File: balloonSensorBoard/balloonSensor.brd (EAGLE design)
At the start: 100 x 80 mm, 36 parts, among them IC1 MCP601OT, IC10 MCP601OT, IC6 MCP601OT, IC7 MCP601OT, U1 ARDUINO-MEGAPRO

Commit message: updated .sch, .brd
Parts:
- removed +9V1: 500 ohm, rcl:R1206
- removed C6, C7: 10uF, resistor:CT3216
- removed LD1085: (no value), v-reg:TO220L1
- removed LED3: (no value), SparkFun:LED3MM
- removed U$3: XBEE-1B3, SparkFun:XBEE-SMD
- added C2: 100nF, resistor:CT3216
- added C3: 10uF, resistor:CT3216
- added JP1: (no value), SparkFun:1X04_LONGPADS
- added LD1117: V_REG_317SMD, SparkFun:SOT223
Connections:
- removed net N$19: +9V1.2, LED3.K
- net +3V3: now also JP1.1, U1.3.3V; no longer U$3.1
- net +9V: now also C2.+, LD1117.3, U1.VIN; no longer C6.+, LD1085.3
- net GND: now also C2.-, C3.-, JP1.4, LD1117.1, U1.GND@4; no longer +9V1.1, C6.-, C7.-, LD1085.1, U$3.10
- net N$13: now also JP1.3; no longer U$3.3
- net N$5: now also JP1.2; no longer U$3.2
- net V+: now also C3.+, LD1117.2; no longer C7.+, LD1085.2, LED3.A
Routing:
- net GND: track 199.9 -> 172.8 mm
- net +9V: track 69.0 -> 50.0 mm
- net N$19: track 4.33 -> 0.00 mm
- net V+: track 207.9 -> 205.4 mm

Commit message: updated .sch, .brd
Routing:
- net GND: track 172.8 -> 118.0 mm
- net +9V: track 50.0 -> 6.21 mm
- net V+: track 205.4 -> 180.5 mm
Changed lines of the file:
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@@
 <wire x1="57.912" y1="44.704" x2="60.198" y2="44.704" width="0.254" layer="16"/>
 <wire x1="57.912" y1="44.704" x2="57.68" y2="44.98" width="0.254" layer="16"/>
-<wire x1="34.544" y1="18.288" x2="22.352" y2="30.48" width="0.254" layer="16"/>
-<wire x1="37.592" y1="18.288" x2="34.544" y2="18.288" width="0.254" layer="16"/>
-<wire x1="22.352" y1="30.48" x2="21.59" y2="30.56" width="0.254" layer="16"/>
 <wire x1="60.96" y1="29.718" x2="60.96" y2="26.706" width="0.254" layer="1"/>
 <wire x1="61.722" y1="30.48" x2="60.96" y2="29.718" width="0.254" layer="1"/>
@@
 <wire x1="34.29" y1="57.15" x2="33.528" y2="56.388" width="0.254" layer="1"/>
 <wire x1="34.29" y1="60.96" x2="34.29" y2="57.15" width="0.254" layer="1"/>
-<wire x1="22.098" y1="28.956" x2="32.004" y2="28.956" width="0.254" layer="1"/>
-<wire x1="32.004" y1="28.956" x2="32.766" y2="28.956" width="0.254" layer="1"/>
-<wire x1="22.098" y1="30.48" x2="22.098" y2="28.956" width="0.254" layer="1"/>
-<wire x1="22.098" y1="30.48" x2="21.59" y2="30.56" width="0.254" layer="1"/>
 <wire x1="34.29" y1="33.528" x2="33.528" y2="34.29" width="0.254" layer="1"/>
 <wire x1="34.29" y1="30.48" x2="34.29" y2="33.528" width="0.254" layer="1"/>
 <wire x1="33.528" y1="29.718" x2="34.29" y2="30.48" width="0.254" layer="1"/>
 <wire x1="33.528" y1="34.29" x2="33.02" y2="34.773" width="0.254" layer="1"/>
-<wire x1="58.674" y1="29.718" x2="57.912" y2="30.48" width="0.254" layer="1"/>
-<wire x1="59.69" y1="20.574" x2="59.436" y2="20.574" width="0.254" layer="1"/>
-<wire x1="58.674" y1="21.5265" x2="58.674" y2="25.146" width="0.254" layer="1"/>
-<wire x1="58.674" y1="25.146" x2="58.674" y2="29.718" width="0.254" layer="1"/>
-<wire x1="57.912" y1="30.48" x2="57.785" y2="30.963" width="0.254" layer="1"/>
-<wire x1="32.004" y1="23.622" x2="32.766" y2="22.86" width="0.254" layer="1"/>
-<wire x1="32.004" y1="28.956" x2="32.004" y2="23.622" width="0.254" layer="1"/>
 <wire x1="34.29" y1="54.864" x2="33.528" y2="55.626" width="0.254" layer="1"/>
 <wire x1="34.29" y1="33.528" x2="34.29" y2="54.864" width="0.254" layer="1"/>
-<wire x1="60.96" y1="25.908" x2="60.96" y2="26.706" width="0.254" layer="1"/>
-<wire x1="60.198" y1="25.146" x2="60.96" y2="25.908" width="0.254" layer="1"/>
-<wire x1="58.674" y1="25.146" x2="60.198" y2="25.146" width="0.254" layer="1"/>
-<wire x1="58.674" y1="21.5265" x2="59.436" y2="20.574" width="0.254" layer="1"/>
 <contactref element="U$1" pad="FIGV+/E2V-"/>
 <contactref element="R2" pad="2"/>
@@
 <wire x1="10.16" y1="-95.25" x2="5.08" y2="-95.25" width="0" layer="19" extent="1-1"/>
 <wire x1="9.42" y1="-70.38" x2="3.81" y2="-82.586" width="0" layer="19" extent="1-1"/>
-<wire x1="34.544" y1="18.288" x2="9.42" y2="-70.38" width="0" layer="19" extent="16-16"/>
-<wire x1="33.528" y1="29.718" x2="32.766" y2="28.956" width="0" layer="19" extent="1-1"/>
+<wire x1="21.59" y1="30.56" x2="9.42" y2="-70.38" width="0" layer="19" extent="1-1"/>
+<wire x1="33.528" y1="29.718" x2="21.59" y2="30.56" width="0" layer="19" extent="1-1"/>
 <wire x1="33.528" y1="56.388" x2="33.528" y2="55.626" width="0" layer="19" extent="1-1"/>
 <wire x1="20.066" y1="62.23" x2="34.29" y2="60.96" width="0" layer="19" extent="1-1"/>
-<wire x1="58.674" y1="21.5265" x2="37.592" y2="18.288" width="0" layer="19" extent="1-16"/>
-<wire x1="60.198" y1="21.59" x2="59.69" y2="20.574" width="0" layer="19" extent="1-16"/>
+<wire x1="57.785" y1="30.963" x2="34.29" y2="30.48" width="0" layer="19" extent="1-1"/>
+<wire x1="60.96" y1="29.718" x2="57.785" y2="30.963" width="0" layer="19" extent="1-1"/>
+<wire x1="60.198" y1="21.59" x2="60.96" y2="26.706" width="0" layer="19" extent="1-16"/>
 </signal>
 <signal name="V+">
@@
 <contactref element="IC7" pad="5"/>
 <contactref element="IC10" pad="5"/>
-<wire x1="42.672" y1="15.24" x2="40.64" y2="17.272" width="0.254" layer="16"/>
-<wire x1="54.737" y1="15.24" x2="42.672" y2="15.24" width="0.254" layer="16"/>
+<wire x1="42.672" y1="15.24" x2="40.64" y2="17.272" width="0" layer="19" extent="1-16"/>
+<wire x1="54.737" y1="15.24" x2="42.672" y2="15.24" width="0" layer="19" extent="1-16"/>
 <wire x1="54.483" y1="16.256" x2="54.737" y2="15.24" width="0.254" layer="16"/>
 <wire x1="28.448" y1="44.704" x2="28.448" y2="41.656" width="0.254" layer="1"/>
@@
 <wire x1="53.848" y1="44.704" x2="54.08" y2="44.98" width="0.254" layer="16"/>
 <wire x1="54.61" y1="15.24" x2="54.737" y2="15.24" width="0.3048" layer="16"/>
-<wire x1="54.737" y1="15.24" x2="64.77" y2="15.24" width="0.3048" layer="16"/>
+<wire x1="54.737" y1="15.24" x2="64.77" y2="15.24" width="0" layer="19" extent="1-16"/>
 <wire x1="64.77" y1="15.24" x2="64.77" y2="23.622" width="0.3048" layer="16"/>
 <wire x1="75.438" y1="31.242" x2="73.152" y2="31.242" width="0.254" layer="1"/>
@@
 <wire x1="21.59" y1="35.56" x2="25.4" y2="35.56" width="0.254" layer="16"/>
 <wire x1="26.416" y1="36.576" x2="27.305" y2="36.195" width="0.254" layer="16"/>
-<wire x1="60.96" y1="18.288" x2="61.976" y2="17.272" width="0.254" layer="16"/>
-<wire x1="43.688" y1="18.288" x2="44.704" y2="18.288" width="0.254" layer="16"/>
-<wire x1="44.704" y1="18.288" x2="60.96" y2="18.288" width="0.254" layer="16"/>
-<wire x1="44.704" y1="18.288" x2="27.432" y2="35.56" width="0.254" layer="16"/>
-<wire x1="27.432" y1="35.56" x2="27.305" y2="36.195" width="0.254" layer="16"/>
 <contactref element="U1" pad="VIN"/>
 <contactref element="C2" pad="+"/>
@@
 <wire x1="-11.6586" y1="-121.2088" x2="-12.57" y2="-125.73" width="0" layer="19" extent="1-1"/>
 <wire x1="39.37" y1="13.97" x2="-11.6586" y2="-121.2088" width="0" layer="19" extent="1-1"/>
-<wire x1="43.688" y1="18.288" x2="39.37" y2="13.97" width="0" layer="19" extent="16-16"/>
+<wire x1="27.305" y1="36.195" x2="39.37" y2="13.97" width="0" layer="19" extent="1-1"/>
 </signal>
 <signal name="N$38">

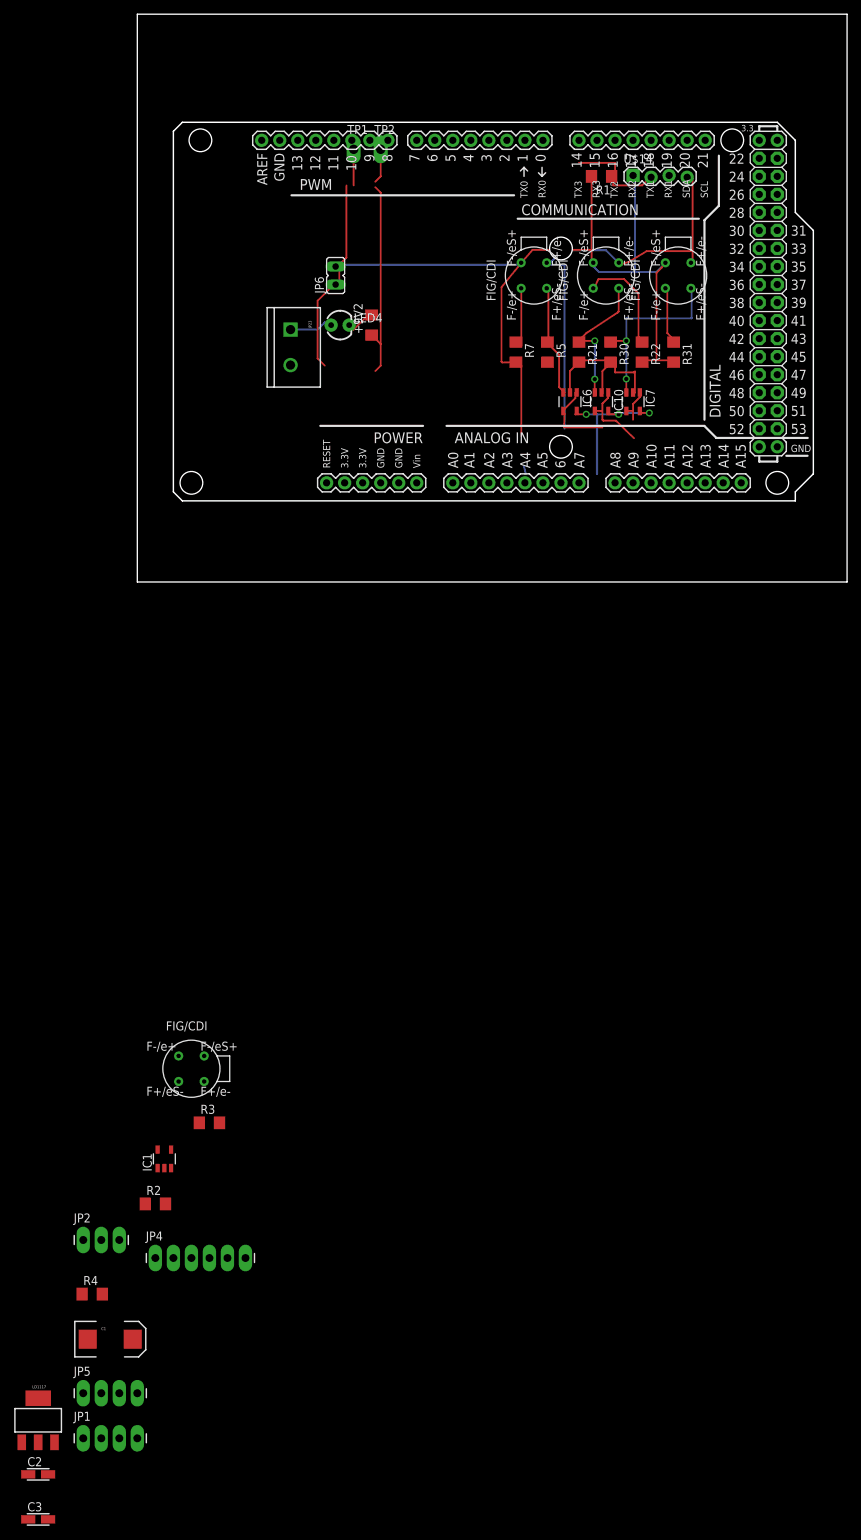
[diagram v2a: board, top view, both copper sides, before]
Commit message: added sensors and miscellaneous parts and routed board
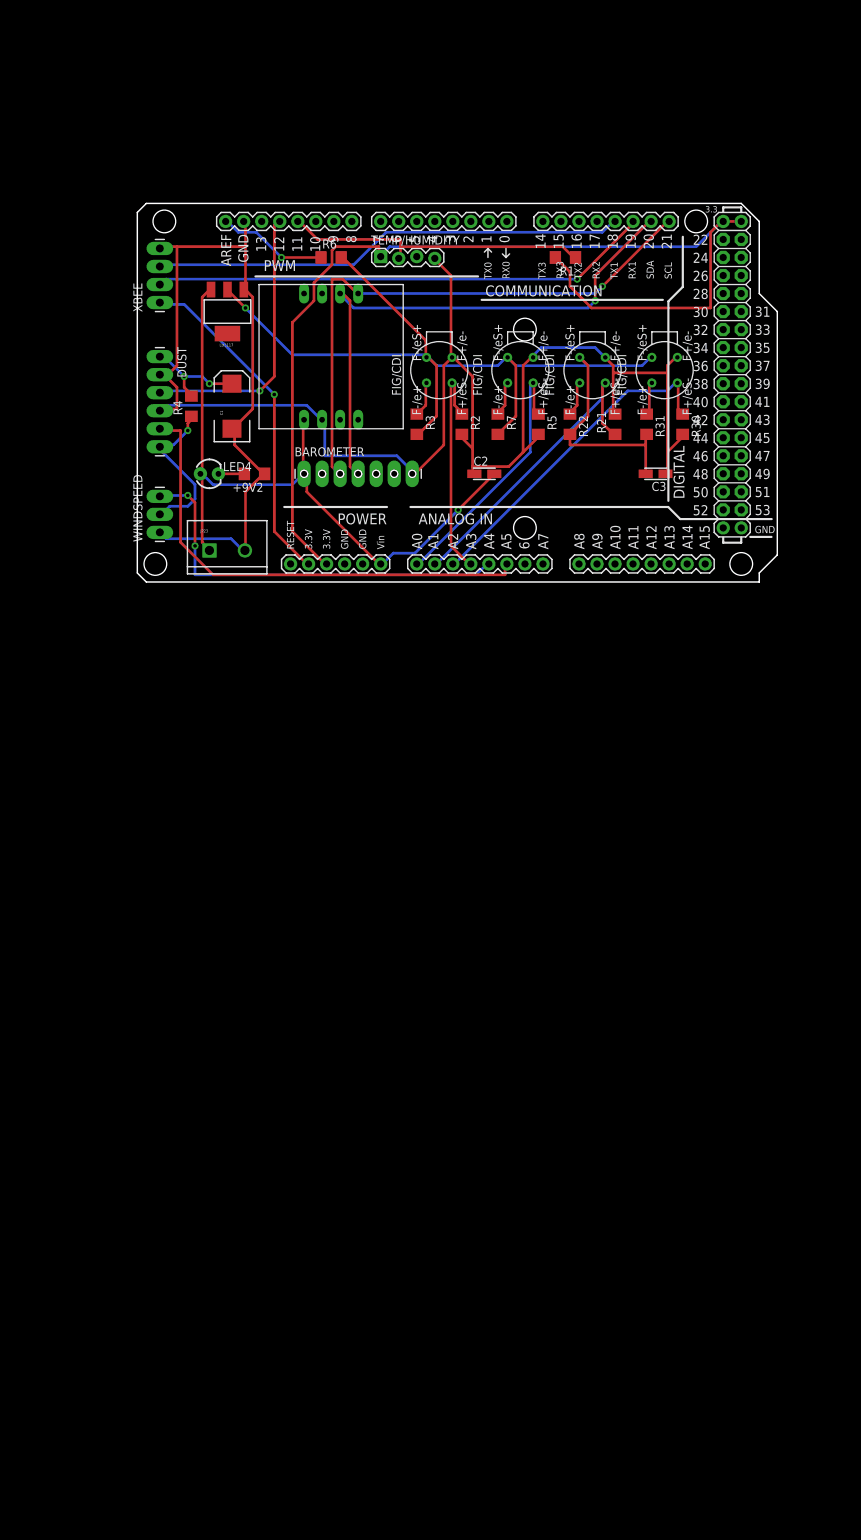
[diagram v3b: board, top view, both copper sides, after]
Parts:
- removed IC1, IC10, IC6, IC7: MCP601OT, linear:SOT23-5
- removed JP1, JP5: (no value), SparkFun:1X04_LONGPADS
- removed JP2: (no value), SparkFun:1X03_LONGPADS
- removed JP4: (no value), SparkFun:1X06_LONGPADS
- removed JP6: (no value), jumper:JP1
- removed TP1, TP2: TPPAD1-13Y, testpad:P1-13Y
- removed U$1, U$9: E2V Ozone, ricardo:SR-4
- removed U$13: E2V, ricardo:SR-4
- removed U$14: RHT03, ricardo:1X04_LOCK
- added BAROMETER: (no value), SparkFun:1X07_LONGPADS
- added CO: E2V, ricardo:SR-4
- added COMPASS: COMPASS, balloonshield:COMPASS
- added DUST: (no value), SparkFun:1X06_LONGPADS
- added O3, VOC: E2V Ozone, ricardo:SR-4
- added R6: 1k, rcl:R1206
- added TEMP/HUMIDITY: RHT03, ricardo:1X04_LOCK
- added WINDSPEED: (no value), SparkFun:1X03_LONGPADS
- added XBEE: (no value), SparkFun:1X04_LONGPADS
- moved C3 171.1 mm to (73.0, 15.2), turned to 180 degrees
- moved LD1117 158.5 mm to (12.7, 38.1), turned to 180 degrees
- moved C2 154.4 mm to (48.9, 15.2)
- moved C1 132.6 mm to (13.3, 24.8), turned to 90 degrees
- moved R4 125.9 mm to (7.62, 24.8), turned to 90 degrees
- moved R2 118.0 mm to (45.7, 22.2), turned to 270 degrees
- moved R3 102.7 mm to (39.4, 22.2), turned to 270 degrees
- moved JP23 33.1 mm to (10.2, 4.45), turned to 0 degrees
- moved LED4 27.9 mm to (10.2, 15.2)
- moved +9V2 26.7 mm to (16.5, 15.2), turned to 180 degrees
- moved R22 14.4 mm to (61.0, 22.2)
- moved R30 14.4 mm to (76.8, 22.2)
- moved NO2 13.5 mm to (54.0, 29.8)
- moved R1 12.5 mm to (60.3, 45.7)
- moved U1 12.5 mm to (0.00, 0.00)
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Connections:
- removed net N$12: JP5.3, U1.20
- removed net N$20: JP5.4, U1.21
- removed net N$48: IC10.1, IC10.4, U1.A1
- removed net N$52: IC6.1, IC6.4, U1.A0
- removed net N$9: IC7.1, IC7.4, U1.A2
- new net 5V: R1.2, TEMP/HUMIDITY.VDD, U1.5V@0, U1.5V@1, U1.5V@2
- new net SCL: BAROMETER.3, COMPASS.SCL, U1.21
- new net SDA: BAROMETER.4, COMPASS.SDA, U1.20
- net +3V3: now also XBEE.1; no longer JP1.1, JP5.2
- net +5V: now also DUST.6, WINDSPEED.2; no longer JP2.2, JP4.6
- net +9V: now also BAROMETER.1, COMPASS.VIN
- net 3: now also TEMP/HUMIDITY.DATA; no longer U$14.DATA
- net GND: now also BAROMETER.7, CO.FIGV+/E2V-, COMPASS.GND, DUST.2, DUST.4, O3.FIGV+/E2V-, TEMP/HUMIDITY.GND, VOC.FIGV+/E2V-, WINDSPEED.1, XBEE.4; no longer IC1.2, IC10.2, IC6.2, IC7.2, JP1.4, JP2.1, JP4.2, JP4.4, JP5.1, TP2.TP, U$1.FIGV+/E2V-, U$13.FIGV+/E2V-, U$14.GND, U$9.FIGV+/E2V-
- net N$1: now also VOC.FIGSIG/E2VH+; no longer U$1.FIGSIG/E2VH+
- net N$10: now also DUST.3; no longer JP4.3
- net N$11: now also DUST.5; no longer JP4.5
- net N$13: now also XBEE.3; no longer JP1.3
- net N$2: now also U1.A3, VOC.FIGV+/E2VSIG; no longer IC1.3, U$1.FIGV+/E2VSIG
- net N$38: now also CO.FIGSIG/E2VH+; no longer U$13.FIGSIG/E2VH+
- net N$4: now also R6.1, U1.AREF; no longer IC1.1, IC1.4, U1.A3
- net N$45: now also O3.FIGSIG/E2VH+; no longer U$9.FIGSIG/E2VH+
- net N$47: now also CO.FIGV+/E2VSIG, U1.A1; no longer IC10.3, U$13.FIGV+/E2VSIG
- net N$5: now also XBEE.2; no longer JP1.2
- net N$50: now also U1.A0; no longer IC6.3
- net N$55: now also O3.FIGV+/E2VSIG, U1.A2; no longer IC7.3, U$9.FIGV+/E2VSIG
- net N$7: now also WINDSPEED.3; no longer JP2.3
- net N$8: now also DUST.1; no longer JP4.1
- net V+: now also CO.FIGG/E2VS+, O3.FIGG/E2VS+, R6.2, VOC.FIGG/E2VS+; no longer IC1.5, IC10.5, IC6.5, IC7.5, JP6.1, JP6.2, R1.2, TP1.TP, U$1.FIGG/E2VS+, U$13.FIGG/E2VS+, U$14.VDD, U$9.FIGG/E2VS+
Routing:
- net GND: track 118.0 -> 277.2 mm
- net 5V: track 0.00 -> 148.9 mm
- net +9V: track 6.21 -> 100.6 mm, vias 0 -> 1
- net SCL: track 0.00 -> 80.5 mm, vias 0 -> 1
- net SDA: track 0.00 -> 78.8 mm, vias 0 -> 1
- net N$5: track 0.00 -> 70.6 mm, vias 0 -> 1
- net N$11: track 0.00 -> 68.1 mm
- net N$13: track 0.00 -> 66.7 mm
- net N$7: track 0.00 -> 57.6 mm, vias 0 -> 2
- net +3V3: track 0.00 -> 47.5 mm, vias 0 -> 1
- net N$10: track 0.00 -> 39.4 mm, vias 0 -> 1
- net V+: track 180.5 -> 141.9 mm, vias 3 -> 1
- net N$2: track 0.00 -> 32.0 mm
- net 3: track 14.6 -> 43.6 mm
- net N$47: track 20.5 -> 44.2 mm, vias 2 -> 0
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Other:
- board size 100 x 80 mm -> 90.2 x 53.3 mm

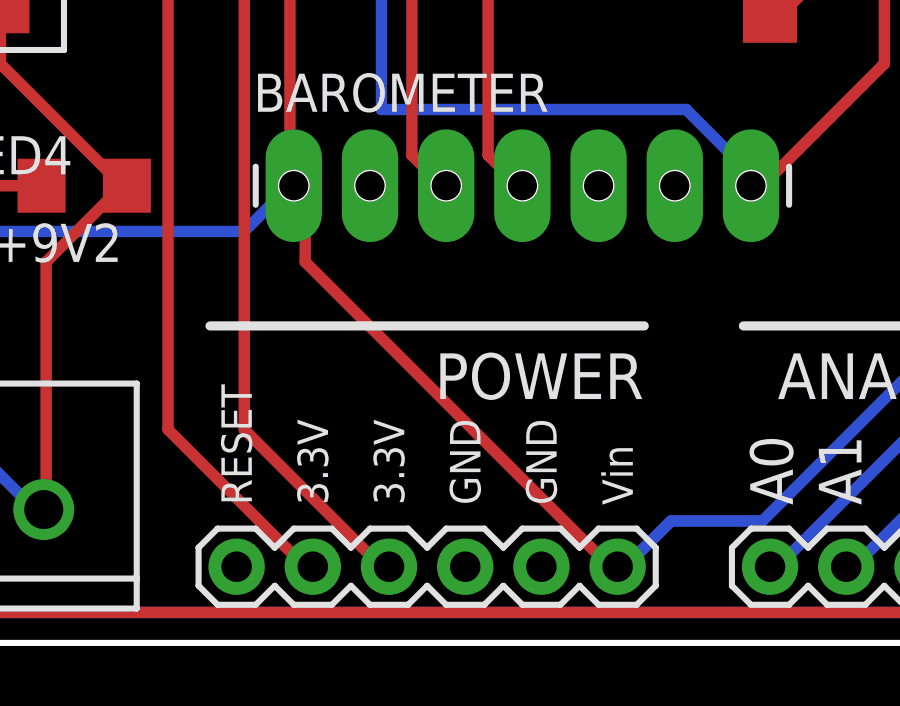
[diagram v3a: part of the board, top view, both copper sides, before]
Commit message: added cap size, mod a couple vins
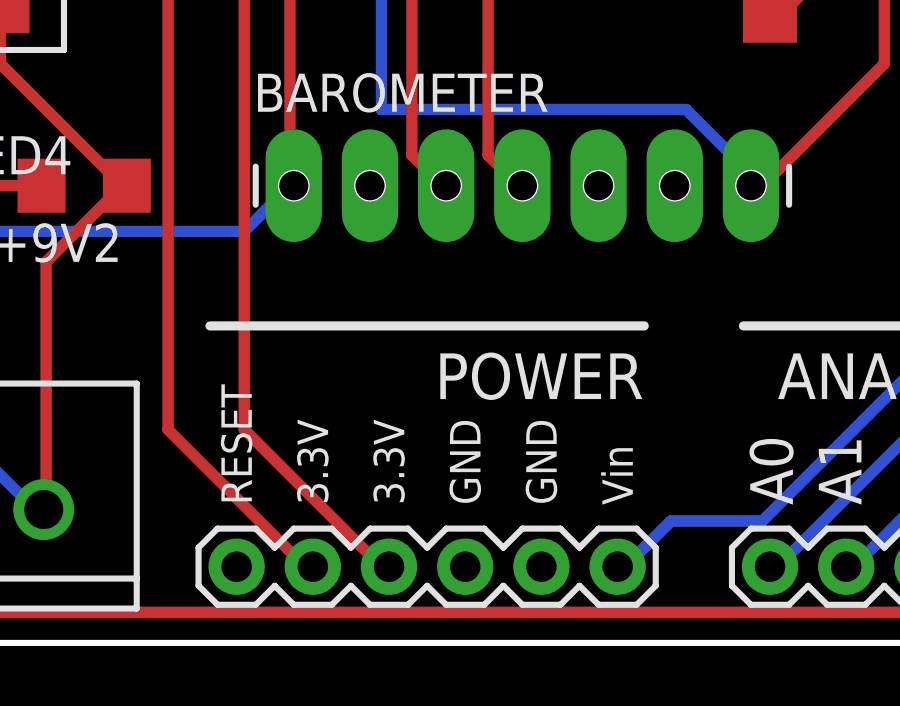
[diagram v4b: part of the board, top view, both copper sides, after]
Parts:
- C1: value (none) -> 220uF
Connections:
- new net VCC: BAROMETER.1, COMPASS.VIN
- net +9V: no longer BAROMETER.1, COMPASS.VIN
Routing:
- net +9V: track 100.6 -> 75.3 mm
- net VCC: track 0.00 -> 7.75 mm
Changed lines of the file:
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@@
 <element name="WINDSPEED" library="SparkFun" package="1X03_LONGPADS" value="" x="3.175" y="6.985" rot="R90"/>
 <element name="R4" library="rcl" package="R1206" value="150ohm" x="7.62" y="24.765" rot="R90"/>
-<element name="C1" library="SparkFun" package="EIA7343" value="" x="13.335" y="24.765" rot="R90"/>
+<element name="C1" library="SparkFun" package="EIA7343" value="220uF" x="13.335" y="24.765" rot="R90"/>
 <element name="XBEE" library="SparkFun" package="1X04_LONGPADS" value="" x="3.175" y="39.37" rot="R90"/>
 <element name="LD1117" library="SparkFun" package="SOT223" value="V_REG_317SMD" x="12.7" y="38.1" rot="R180"/>
@@
 <contactref element="C2" pad="+"/>
 <contactref element="LD1117" pad="3"/>
-<contactref element="BAROMETER" pad="1"/>
-<contactref element="COMPASS" pad="VIN"/>
 <wire x1="45.212" y1="10.16" x2="50.292" y2="15.24" width="0.381" layer="1"/>
 <wire x1="39.116" y1="4.064" x2="45.212" y2="10.16" width="0.381" layer="16"/>
@@
 <wire x1="50.292" y1="15.24" x2="50.295" y2="15.24" width="0.381" layer="1"/>
 <wire x1="34.544" y1="2.54" x2="34.29" y2="2.54" width="0.381" layer="16"/>
-<wire x1="23.368" y1="15.24" x2="23.368" y2="22.86" width="0.381" layer="1"/>
-<wire x1="23.368" y1="22.86" x2="23.495" y2="22.86" width="0.381" layer="1"/>
-<wire x1="23.368" y1="15.24" x2="23.495" y2="15.24" width="0.381" layer="1"/>
 <wire x1="9.144" y1="40.132" x2="10.16" y2="41.148" width="0.381" layer="1"/>
 <wire x1="9.144" y1="15.24" x2="9.144" y2="40.132" width="0.381" layer="1"/>
@@
 <wire x1="10.668" y1="13.716" x2="21.844" y2="13.716" width="0.381" layer="16"/>
 <wire x1="9.144" y1="15.24" x2="10.668" y2="13.716" width="0.381" layer="16"/>
-<wire x1="23.368" y1="15.24" x2="23.495" y2="15.24" width="0.381" layer="16"/>
 <wire x1="9.144" y1="15.24" x2="8.89" y2="15.24" width="0.381" layer="16"/>
-<wire x1="23.876" y1="12.7" x2="34.036" y2="2.54" width="0.381" layer="1"/>
-<wire x1="23.876" y1="15.24" x2="23.876" y2="12.7" width="0.381" layer="1"/>
+<wire x1="23.876" y1="12.7" x2="34.036" y2="2.54" width="0" layer="19" extent="1-16"/>
+<wire x1="23.876" y1="15.24" x2="23.876" y2="12.7" width="0" layer="19" extent="1-16"/>
 <wire x1="34.036" y1="2.54" x2="34.29" y2="2.54" width="0.381" layer="1"/>
-<wire x1="23.876" y1="15.24" x2="23.495" y2="15.24" width="0.381" layer="1"/>
 <via x="45.212" y="10.16" extent="1-16" drill="0.508"/>
+<wire x1="23.368" y1="15.24" x2="23.876" y2="15.24" width="0" layer="19" extent="1-16"/>
 </signal>
 <signal name="N$38">
@@
 <via x="20.32" y="45.72" extent="1-16" drill="0.508"/>
 </signal>
+<signal name="VCC">
+<contactref element="BAROMETER" pad="1"/>
+<contactref element="COMPASS" pad="VIN"/>
+<wire x1="23.368" y1="15.24" x2="23.368" y2="22.86" width="0.381" layer="1"/>
+<wire x1="23.368" y1="22.86" x2="23.495" y2="22.86" width="0.381" layer="1"/>
+<wire x1="23.368" y1="15.24" x2="23.495" y2="15.24" width="0" layer="19" extent="1-1"/>
+</signal>
 </signals>
